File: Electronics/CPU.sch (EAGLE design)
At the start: 12 parts

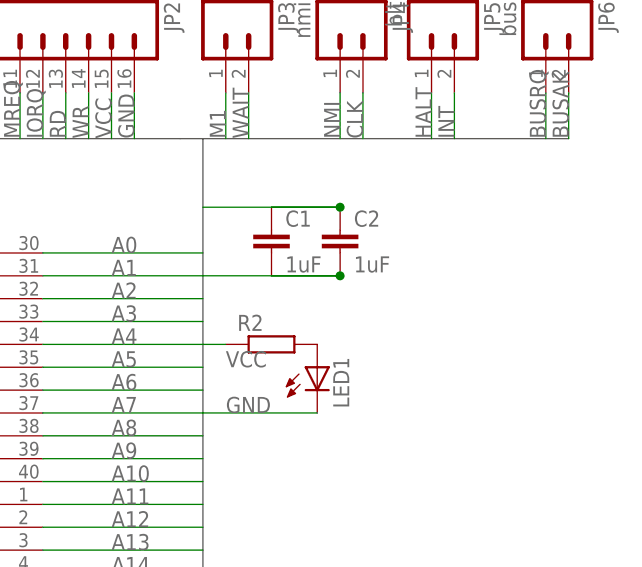
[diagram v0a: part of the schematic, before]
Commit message: Update board outlines
Adding white line around boards for de-panelization
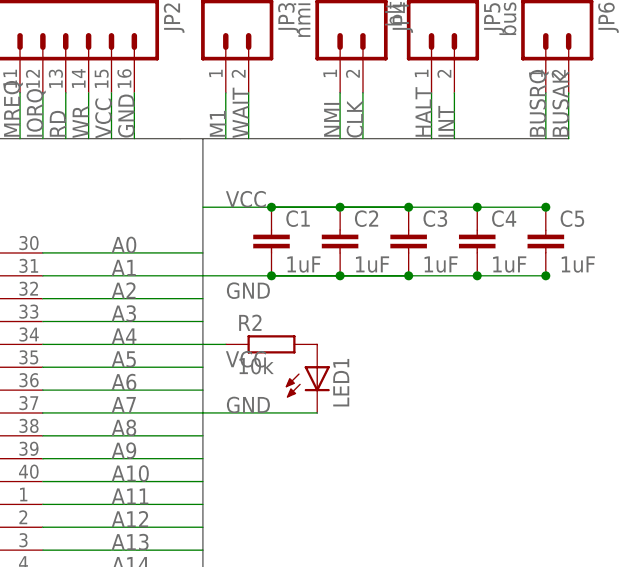
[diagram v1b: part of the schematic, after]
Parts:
- added C3, C4, C5: 1uF, rcl:C-EUC0805
- R2: value (none) -> 10k
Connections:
- net GND: now also C3.2, C4.2, C5.2
- net VCC: now also C3.1, C4.1, C5.1
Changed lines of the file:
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@@
 <part name="R1" library="rcl" deviceset="R-EU_" device="M0805" value="10K"/>
 <part name="C2" library="rcl" deviceset="C-EU" device="C0805" value="1uF"/>
-<part name="R2" library="rcl" deviceset="R-EU_" device="M0805"/>
+<part name="R2" library="rcl" deviceset="R-EU_" device="M0805" value="10k"/>
 <part name="LED1" library="adafruit" deviceset="LED" device="CHIP-LED0805"/>
+<part name="C3" library="rcl" deviceset="C-EU" device="C0805" value="1uF"/>
+<part name="C4" library="rcl" deviceset="C-EU" device="C0805" value="1uF"/>
+<part name="C5" library="rcl" deviceset="C-EU" device="C0805" value="1uF"/>
 </parts>
 <sheets>
@@
 <instance part="R2" gate="G$1" x="109.22" y="78.74"/>
 <instance part="LED1" gate="G$1" x="114.3" y="76.2"/>
+<instance part="C3" gate="G$1" x="124.46" y="91.44"/>
+<instance part="C4" gate="G$1" x="132.08" y="91.44"/>
+<instance part="C5" gate="G$1" x="139.7" y="91.44"/>
 </instances>
 <busses>
@@
 <segment>
 <pinref part="C1" gate="G$1" pin="1"/>
-<wire x1="116.84" y1="93.98" x2="101.6" y2="93.98" width="0.1524" layer="91"/>
 <pinref part="C2" gate="G$1" pin="1"/>
+<junction x="139.7" y="93.98"/>
+<pinref part="C3" gate="G$1" pin="1"/>
+<pinref part="C4" gate="G$1" pin="1"/>
+<pinref part="C5" gate="G$1" pin="1"/>
+<wire x1="116.84" y1="93.98" x2="109.22" y2="93.98" width="0.1524" layer="91"/>
+<wire x1="109.22" y1="93.98" x2="101.6" y2="93.98" width="0.1524" layer="91"/>
+<wire x1="116.84" y1="93.98" x2="109.22" y2="93.98" width="0.1524" layer="91"/>
+<wire x1="139.7" y1="93.98" x2="132.08" y2="93.98" width="0.1524" layer="91"/>
+<junction x="132.08" y="93.98"/>
+<wire x1="132.08" y1="93.98" x2="124.46" y2="93.98" width="0.1524" layer="91"/>
 <junction x="116.84" y="93.98"/>
-<wire x1="116.84" y1="93.98" x2="109.22" y2="93.98" width="0.1524" layer="91"/>
+<wire x1="124.46" y1="93.98" x2="116.84" y2="93.98" width="0.1524" layer="91"/>
+<wire x1="116.84" y1="93.98" x2="124.46" y2="93.98" width="0.1524" layer="91"/>
+<junction x="124.46" y="93.98"/>
+<junction x="109.22" y="93.98"/>
+<label x="104.14" y="93.98" size="1.778" layer="95"/>
 </segment>
 <segment>
@@
 <segment>
 <pinref part="C1" gate="G$1" pin="2"/>
-<wire x1="116.84" y1="86.36" x2="101.6" y2="86.36" width="0.1524" layer="91"/>
 <pinref part="C2" gate="G$1" pin="2"/>
+<junction x="139.7" y="86.36"/>
+<pinref part="C3" gate="G$1" pin="2"/>
+<pinref part="C4" gate="G$1" pin="2"/>
+<pinref part="C5" gate="G$1" pin="2"/>
+<wire x1="116.84" y1="86.36" x2="109.22" y2="86.36" width="0.1524" layer="91"/>
+<wire x1="109.22" y1="86.36" x2="101.6" y2="86.36" width="0.1524" layer="91"/>
+<wire x1="116.84" y1="86.36" x2="109.22" y2="86.36" width="0.1524" layer="91"/>
+<wire x1="139.7" y1="86.36" x2="132.08" y2="86.36" width="0.1524" layer="91"/>
+<junction x="132.08" y="86.36"/>
+<wire x1="132.08" y1="86.36" x2="124.46" y2="86.36" width="0.1524" layer="91"/>
 <junction x="116.84" y="86.36"/>
-<wire x1="116.84" y1="86.36" x2="109.22" y2="86.36" width="0.1524" layer="91"/>
-</segment>
-<segment>
+<wire x1="124.46" y1="86.36" x2="116.84" y2="86.36" width="0.1524" layer="91"/>
+<wire x1="116.84" y1="86.36" x2="124.46" y2="86.36" width="0.1524" layer="91"/>
+<junction x="124.46" y="86.36"/>
+<junction x="109.22" y="86.36"/>
+<label x="104.14" y="83.82" size="1.778" layer="95"/>
+</segment>
+<segment>
